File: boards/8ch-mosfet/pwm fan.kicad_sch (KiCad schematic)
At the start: 2 parts, among them M1 Fan_4pin

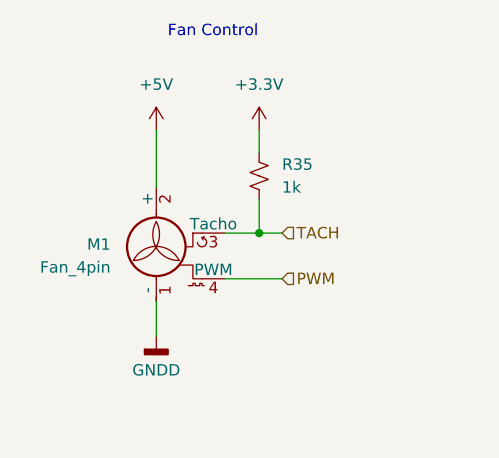
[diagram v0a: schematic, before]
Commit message: more or less placed all the stuff that needs to be placed
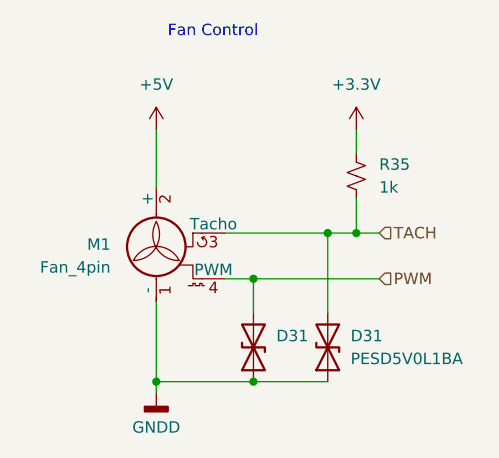
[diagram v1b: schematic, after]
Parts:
- added D31 (x2): PESD5V0L1BA, Diode_SMD:D_SOD-323_HandSoldering, symbol Device:D_TVS
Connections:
- net GNDD: now also D31.1 (A1), D31.1 (A1)
- net PWM: now also D31.2 (A2)
- net TACH: now also D31.2 (A2)
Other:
- moved on the sheet: R35
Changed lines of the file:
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@@
 (kicad_sch (version 20230121) (generator eeschema)
   (paper "A4")
-  (junction (at 144.78 85.09) (diameter 0) (color 0 0 0 0)
-  )
-  (wire (pts (xy 140.97 85.09) (xy 144.78 85.09))
-    (stroke (width 0) (type default))
-  )
-  (wire (pts (xy 144.78 85.09) (xy 147.32 85.09))
-    (stroke (width 0) (type default))
-  )
-  (wire (pts (xy 140.97 90.17) (xy 147.32 90.17))
-    (stroke (width 0) (type default))
-  )
-  (wire (pts (xy 144.78 81.28) (xy 144.78 85.09))
-    (stroke (width 0) (type default))
-  )
-  (wire (pts (xy 133.35 92.71) (xy 133.35 96.52))
-    (stroke (width 0) (type default))
-  )
-  (wire (pts (xy 144.78 76.2) (xy 144.78 73.66))
+  (junction (at 144.145 101.6) (diameter 0) (color 0 0 0 0)
+  )
+  (junction (at 152.4 85.09) (diameter 0) (color 0 0 0 0)
+  )
+  (junction (at 144.145 90.17) (diameter 0) (color 0 0 0 0)
+  )
+  (junction (at 155.575 85.09) (diameter 0) (color 0 0 0 0)
+  )
+  (junction (at 133.35 101.6) (diameter 0) (color 0 0 0 0)
+  )
+  (wire (pts (xy 152.4 85.09) (xy 155.575 85.09))
+    (stroke (width 0) (type default))
+  )
+  (wire (pts (xy 140.97 85.09) (xy 152.4 85.09))
+    (stroke (width 0) (type default))
+  )
+  (wire (pts (xy 155.575 85.09) (xy 158.115 85.09))
+    (stroke (width 0) (type default))
+  )
+  (wire (pts (xy 140.97 90.17) (xy 144.145 90.17))
+    (stroke (width 0) (type default))
+  )
+  (wire (pts (xy 155.575 81.28) (xy 155.575 85.09))
+    (stroke (width 0) (type default))
+  )
+  (wire (pts (xy 144.145 90.17) (xy 158.115 90.17))
+    (stroke (width 0) (type default))
+  )
+  (wire (pts (xy 144.145 101.6) (xy 152.4 101.6))
+    (stroke (width 0) (type default))
+  )
+  (wire (pts (xy 144.145 90.17) (xy 144.145 93.98))
+    (stroke (width 0) (type default))
+  )
+  (wire (pts (xy 133.35 92.71) (xy 133.35 101.6))
+    (stroke (width 0) (type default))
+  )
+  (wire (pts (xy 133.35 101.6) (xy 133.35 102.87))
+    (stroke (width 0) (type default))
+  )
+  (wire (pts (xy 155.575 76.2) (xy 155.575 73.66))
+    (stroke (width 0) (type default))
+  )
+  (wire (pts (xy 133.35 101.6) (xy 144.145 101.6))
     (stroke (width 0) (type default))
   )
   (wire (pts (xy 133.35 73.66) (xy 133.35 80.01))
+    (stroke (width 0) (type default))
+  )
+  (wire (pts (xy 152.4 85.09) (xy 152.4 93.98))
     (stroke (width 0) (type default))
   )
@@
     (effects (font (size 1.27 1.27)) (justify left bottom))
   )
-  (hierarchical_label "TACH" (shape input) (at 147.32 85.09 0) (fields_autoplaced)
+  (hierarchical_label "TACH" (shape input) (at 158.115 85.09 0) (fields_autoplaced)
     (effects (font (size 1.27 1.27)) (justify left))
   )
-  (hierarchical_label "PWM" (shape input) (at 147.32 90.17 0) (fields_autoplaced)
+  (hierarchical_label "PWM" (shape input) (at 158.115 90.17 0) (fields_autoplaced)
     (effects (font (size 1.27 1.27)) (justify left))
   )
-  (symbol (lib_id "Device:R_Small_US") (at 144.78 78.74 180) (unit 1)
+  (symbol (lib_id "Device:R_Small_US") (at 155.575 78.74 180) (unit 1)
     (in_bom yes) (on_board yes) (dnp no) (fields_autoplaced)
-    (property "Reference" "R35" (at 147.32 77.47 0)
-      (effects (font (size 1.27 1.27)) (justify right))
-    )
-    (property "Value" "1k" (at 147.32 80.01 0)
-      (effects (font (size 1.27 1.27)) (justify right))
-    )
-    (property "Footprint" "Resistor_SMD:R_0805_2012Metric_Pad1.20x1.40mm_HandSolder" (at 144.78 78.74 0)
-      (effects (font (size 1.27 1.27)) hide)
-    )
-    (property "Datasheet" "~" (at 144.78 78.74 0)
-      (effects (font (size 1.27 1.27)) hide)
-    )
-    (property "Vendor" "652-CR0805JW-103ELF" (at 144.78 78.74 0)
+    (property "Reference" "R35" (at 158.115 77.47 0)
+      (effects (font (size 1.27 1.27)) (justify right))
+    )
+    (property "Value" "1k" (at 158.115 80.01 0)
+      (effects (font (size 1.27 1.27)) (justify right))
+    )
+    (property "Footprint" "Resistor_SMD:R_0805_2012Metric_Pad1.20x1.40mm_HandSolder" (at 155.575 78.74 0)
+      (effects (font (size 1.27 1.27)) hide)
+    )
+    (property "Datasheet" "~" (at 155.575 78.74 0)
+      (effects (font (size 1.27 1.27)) hide)
+    )
+    (property "Vendor" "652-CR0805JW-103ELF" (at 155.575 78.74 0)
       (effects (font (size 1.27 1.27)) hide)
     )
@@
     )
   )
-  (symbol (lib_id "power:+3.3V") (at 144.78 73.66 0) (unit 1)
+  (symbol (lib_id "Device:D_TVS") (at 144.145 97.79 90) (unit 1)
+    (in_bom yes) (on_board yes) (dnp no)
+    (property "Reference" "D31" (at 146.685 96.52 90)
+      (effects (font (size 1.27 1.27)) (justify right))
+    )
+    (property "Value" "PESD5V0L1BA" (at 154.94 99.06 90)
+      (effects (font (size 1.27 1.27)) (justify right) hide)
+    )
+    (property "Footprint" "Diode_SMD:D_SOD-323_HandSoldering" (at 144.145 97.79 0)
+      (effects (font (size 1.27 1.27)) hide)
+    )
+    (property "Datasheet" "~" (at 144.145 97.79 0)
+      (effects (font (size 1.27 1.27)) hide)
+    )
+    (pin "1")
+    (pin "2")
+    (instances
+      (project "8ch-mosfet"
+        (path "/c83c6236-96e9-46ad-9d7a-9e2efa4a7966/0036d08f-39b5-4a29-8e4d-ea832b2cc879"
+          (reference "D31") (unit 1)
+        )
+        (path "/c83c6236-96e9-46ad-9d7a-9e2efa4a7966/e112a34f-fd2f-43cb-bf5d-a7f5e57b6bef"
+          (reference "D32") (unit 1)
+        )
+        (path "/c83c6236-96e9-46ad-9d7a-9e2efa4a7966/ad82ad0c-2ba8-4934-bb2a-ed6e11658eb2"
+          (reference "D34") (unit 1)
+        )
+        (path "/c83c6236-96e9-46ad-9d7a-9e2efa4a7966/02f6e629-b0e2-41e8-b2e4-f0e125a92a71"
+          (reference "D35") (unit 1)
+        )
+      )
+    )
+  )
+  (symbol (lib_id "power:+3.3V") (at 155.575 73.66 0) (unit 1)
     (in_bom yes) (on_board yes) (dnp no) (fields_autoplaced)
-    (property "Reference" "#PWR064" (at 144.78 77.47 0)
-      (effects (font (size 1.27 1.27)) hide)
-    )
-    (property "Value" "+3.3V" (at 144.78 68.58 0)
+    (property "Reference" "#PWR064" (at 155.575 77.47 0)
+      (effects (font (size 1.27 1.27)) hide)
+    )
+    (property "Value" "+3.3V" (at 155.575 68.58 0)
       (effects (font (size 1.27 1.27)))
     )
-    (property "Footprint" "" (at 144.78 73.66 0)
-      (effects (font (size 1.27 1.27)) hide)
-    )
-    (property "Datasheet" "" (at 144.78 73.66 0)
+    (property "Footprint" "" (at 155.575 73.66 0)
+      (effects (font (size 1.27 1.27)) hide)
+    )
+    (property "Datasheet" "" (at 155.575 73.66 0)
       (effects (font (size 1.27 1.27)) hide)
     )
@@
     )
   )
-  (symbol (lib_id "power:GNDD") (at 133.35 96.52 0) (unit 1)
+  (symbol (lib_id "power:GNDD") (at 133.35 102.87 0) (unit 1)
     (in_bom yes) (on_board yes) (dnp no) (fields_autoplaced)
-    (property "Reference" "#PWR08" (at 133.35 102.87 0)
-      (effects (font (size 1.27 1.27)) hide)
-    )
-    (property "Value" "GNDD" (at 133.35 100.33 0)
+    (property "Reference" "#PWR08" (at 133.35 109.22 0)
+      (effects (font (size 1.27 1.27)) hide)
+    )
+    (property "Value" "GNDD" (at 133.35 106.68 0)
       (effects (font (size 1.27 1.27)))
     )
-    (property "Footprint" "" (at 133.35 96.52 0)
-      (effects (font (size 1.27 1.27)) hide)
-    )
-    (property "Datasheet" "" (at 133.35 96.52 0)
+    (property "Footprint" "" (at 133.35 102.87 0)
+      (effects (font (size 1.27 1.27)) hide)
+    )
+    (property "Datasheet" "" (at 133.35 102.87 0)
       (effects (font (size 1.27 1.27)) hide)
     )
@@
         )
       )
+    )
+  )
+  (symbol (lib_id "Device:D_TVS") (at 152.4 97.79 90) (unit 1)
+    (in_bom yes) (on_board yes) (dnp no)
+    (property "Reference" "D31" (at 154.94 96.52 90)
+      (effects (font (size 1.27 1.27)) (justify right))
+    )
+    (property "Value" "PESD5V0L1BA" (at 154.94 99.06 90)
+      (effects (font (size 1.27 1.27)) (justify right))
+    )
+    (property "Footprint" "Diode_SMD:D_SOD-323_HandSoldering" (at 152.4 97.79 0)
+      (effects (font (size 1.27 1.27)) hide)
+    )
+    (property "Datasheet" "~" (at 152.4 97.79 0)
+      (effects (font (size 1.27 1.27)) hide)
+    )
+    (pin "1")
+    (pin "2")
+    (instances
+      (project "8ch-mosfet"
+        (path "/c83c6236-96e9-46ad-9d7a-9e2efa4a7966/0036d08f-39b5-4a29-8e4d-ea832b2cc879"
+          (reference "D31") (unit 1)
+        )
+        (path "/c83c6236-96e9-46ad-9d7a-9e2efa4a7966/e112a34f-fd2f-43cb-bf5d-a7f5e57b6bef"
+          (reference "D32") (unit 1)
+        )
+        (path "/c83c6236-96e9-46ad-9d7a-9e2efa4a7966/ad82ad0c-2ba8-4934-bb2a-ed6e11658eb2"
+          (reference "D36") (unit 1)
+        )
+        (path "/c83c6236-96e9-46ad-9d7a-9e2efa4a7966/02f6e629-b0e2-41e8-b2e4-f0e125a92a71"
+          (reference "D37") (unit 1)
+        )
+      )

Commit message: added in reverse polarity diode to power circuit
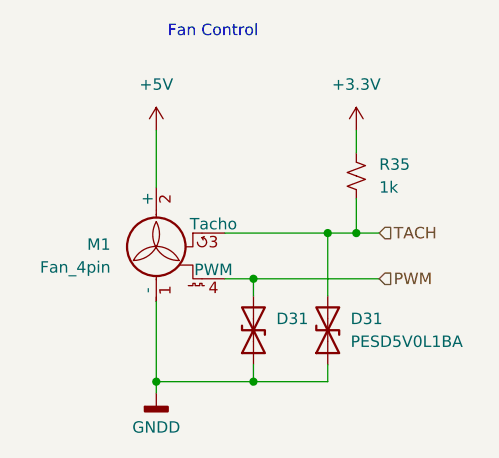
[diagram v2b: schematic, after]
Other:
- moved on the sheet: D31
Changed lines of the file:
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@@
+    (stroke (width 0) (type default))
+  )
+  (wire (pts (xy 152.4 101.6) (xy 152.4 99.695))
     (stroke (width 0) (type default))
   )
@@
     (stroke (width 0) (type default))
   )
+  (wire (pts (xy 144.145 99.695) (xy 144.145 101.6))
+    (stroke (width 0) (type default))
+  )
   (wire (pts (xy 144.145 101.6) (xy 152.4 101.6))
     (stroke (width 0) (type default))
   )
-  (wire (pts (xy 144.145 90.17) (xy 144.145 93.98))
+  (wire (pts (xy 144.145 90.17) (xy 144.145 92.075))
     (stroke (width 0) (type default))
   )
@@
     (stroke (width 0) (type default))
   )
-  (wire (pts (xy 152.4 85.09) (xy 152.4 93.98))
+  (wire (pts (xy 152.4 85.09) (xy 152.4 92.075))
     (stroke (width 0) (type default))
   )
@@
     )
   )
-  (symbol (lib_id "Device:D_TVS") (at 144.145 97.79 90) (unit 1)
+  (symbol (lib_id "Device:D_TVS") (at 144.145 95.885 90) (unit 1)
     (in_bom yes) (on_board yes) (dnp no)
-    (property "Reference" "D31" (at 146.685 96.52 90)
-      (effects (font (size 1.27 1.27)) (justify right))
-    )
-    (property "Value" "PESD5V0L1BA" (at 154.94 99.06 90)
+    (property "Reference" "D31" (at 146.685 94.615 90)
+      (effects (font (size 1.27 1.27)) (justify right))
+    )
+    (property "Value" "PESD5V0L1BA" (at 154.94 97.155 90)
       (effects (font (size 1.27 1.27)) (justify right) hide)
     )
-    (property "Footprint" "Diode_SMD:D_SOD-323_HandSoldering" (at 144.145 97.79 0)
-      (effects (font (size 1.27 1.27)) hide)
-    )
-    (property "Datasheet" "~" (at 144.145 97.79 0)
+    (property "Footprint" "Diode_SMD:D_SOD-323_HandSoldering" (at 144.145 95.885 0)
+      (effects (font (size 1.27 1.27)) hide)
+    )
+    (property "Datasheet" "~" (at 144.145 95.885 0)
       (effects (font (size 1.27 1.27)) hide)
     )
@@
     )
   )
-  (symbol (lib_id "Device:D_TVS") (at 152.4 97.79 90) (unit 1)
+  (symbol (lib_id "Device:D_TVS") (at 152.4 95.885 90) (unit 1)
     (in_bom yes) (on_board yes) (dnp no)
-    (property "Reference" "D31" (at 154.94 96.52 90)
-      (effects (font (size 1.27 1.27)) (justify right))
-    )
-    (property "Value" "PESD5V0L1BA" (at 154.94 99.06 90)
-      (effects (font (size 1.27 1.27)) (justify right))
-    )
-    (property "Footprint" "Diode_SMD:D_SOD-323_HandSoldering" (at 152.4 97.79 0)
-      (effects (font (size 1.27 1.27)) hide)
-    )
-    (property "Datasheet" "~" (at 152.4 97.79 0)
-      (effects (font (size 1.27 1.27)) hide)
-    )
+    (property "Reference" "D31" (at 154.94 94.615 90)
+      (effects (font (size 1.27 1.27)) (justify right))
+    )
+    (property "Value" "PESD5V0L1BA" (at 154.94 97.155 90)
+      (effects (font (size 1.27 1.27)) (justify right))
+    )
+    (property "Footprint" "Diode_SMD:D_SOD-323_HandSoldering" (at 152.4 95.885 0)
+      (effects (font (size 1.27 1.27)) hide)
+    )
+    (property "Datasheet" "~" (at 152.4 95.885 0)
+      (effects (font (size 1.27 1.27)) hide)
+    )

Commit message: tidied up the schematic
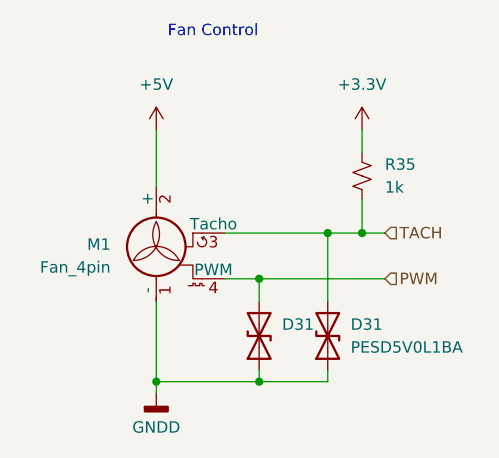
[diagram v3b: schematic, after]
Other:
- moved on the sheet: D31, R35
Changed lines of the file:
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@@
 (kicad_sch (version 20230121) (generator eeschema)
   (paper "A4")
-  (junction (at 144.145 101.6) (diameter 0) (color 0 0 0 0)
+  (junction (at 144.78 90.17) (diameter 0) (color 0 0 0 0)
+  )
+  (junction (at 144.78 101.6) (diameter 0) (color 0 0 0 0)
   )
   (junction (at 152.4 85.09) (diameter 0) (color 0 0 0 0)
   )
-  (junction (at 144.145 90.17) (diameter 0) (color 0 0 0 0)
-  )
-  (junction (at 155.575 85.09) (diameter 0) (color 0 0 0 0)
+  (junction (at 156.21 85.09) (diameter 0) (color 0 0 0 0)
   )
   (junction (at 133.35 101.6) (diameter 0) (color 0 0 0 0)
   )
-  (wire (pts (xy 152.4 85.09) (xy 155.575 85.09))
+  (wire (pts (xy 144.78 101.6) (xy 152.4 101.6))
+    (stroke (width 0) (type default))
+  )
+  (wire (pts (xy 152.4 85.09) (xy 156.21 85.09))
     (stroke (width 0) (type default))
   )
@@
     (stroke (width 0) (type default))
   )
-  (wire (pts (xy 152.4 101.6) (xy 152.4 99.695))
-    (stroke (width 0) (type default))
-  )
-  (wire (pts (xy 155.575 85.09) (xy 158.115 85.09))
-    (stroke (width 0) (type default))
-  )
-  (wire (pts (xy 140.97 90.17) (xy 144.145 90.17))
-    (stroke (width 0) (type default))
-  )
-  (wire (pts (xy 155.575 81.28) (xy 155.575 85.09))
-    (stroke (width 0) (type default))
-  )
-  (wire (pts (xy 144.145 90.17) (xy 158.115 90.17))
-    (stroke (width 0) (type default))
-  )
-  (wire (pts (xy 144.145 99.695) (xy 144.145 101.6))
-    (stroke (width 0) (type default))
-  )
-  (wire (pts (xy 144.145 101.6) (xy 152.4 101.6))
-    (stroke (width 0) (type default))
-  )
-  (wire (pts (xy 144.145 90.17) (xy 144.145 92.075))
+  (wire (pts (xy 152.4 101.6) (xy 152.4 100.33))
+    (stroke (width 0) (type default))
+  )
+  (wire (pts (xy 140.97 90.17) (xy 144.78 90.17))
+    (stroke (width 0) (type default))
+  )
+  (wire (pts (xy 156.21 81.28) (xy 156.21 85.09))
+    (stroke (width 0) (type default))
+  )
+  (wire (pts (xy 144.78 100.33) (xy 144.78 101.6))
+    (stroke (width 0) (type default))
+  )
+  (wire (pts (xy 156.21 85.09) (xy 158.75 85.09))
+    (stroke (width 0) (type default))
+  )
+  (wire (pts (xy 144.78 90.17) (xy 158.75 90.17))
+    (stroke (width 0) (type default))
+  )
+  (wire (pts (xy 144.78 90.17) (xy 144.78 92.71))
     (stroke (width 0) (type default))
   )
@@
     (stroke (width 0) (type default))
   )
-  (wire (pts (xy 155.575 76.2) (xy 155.575 73.66))
-    (stroke (width 0) (type default))
-  )
-  (wire (pts (xy 133.35 101.6) (xy 144.145 101.6))
+  (wire (pts (xy 156.21 73.66) (xy 156.21 76.2))
+    (stroke (width 0) (type default))
+  )
+  (wire (pts (xy 133.35 101.6) (xy 144.78 101.6))
     (stroke (width 0) (type default))
   )
@@
     (stroke (width 0) (type default))
   )
-  (wire (pts (xy 152.4 85.09) (xy 152.4 92.075))
+  (wire (pts (xy 152.4 85.09) (xy 152.4 92.71))
     (stroke (width 0) (type default))
   )
@@
     (effects (font (size 1.27 1.27)) (justify left bottom))
   )
-  (hierarchical_label "TACH" (shape input) (at 158.115 85.09 0) (fields_autoplaced)
+  (hierarchical_label "TACH" (shape input) (at 158.75 85.09 0) (fields_autoplaced)
     (effects (font (size 1.27 1.27)) (justify left))
   )
-  (hierarchical_label "PWM" (shape input) (at 158.115 90.17 0) (fields_autoplaced)
+  (hierarchical_label "PWM" (shape input) (at 158.75 90.17 0) (fields_autoplaced)
     (effects (font (size 1.27 1.27)) (justify left))
   )
-  (symbol (lib_id "Device:R_Small_US") (at 155.575 78.74 180) (unit 1)
-    (in_bom yes) (on_board yes) (dnp no) (fields_autoplaced)
-    (property "Reference" "R35" (at 158.115 77.47 0)
-      (effects (font (size 1.27 1.27)) (justify right))
-    )
-    (property "Value" "1k" (at 158.115 80.01 0)
-      (effects (font (size 1.27 1.27)) (justify right))
-    )
-    (property "Footprint" "Resistor_SMD:R_0805_2012Metric_Pad1.20x1.40mm_HandSolder" (at 155.575 78.74 0)
-      (effects (font (size 1.27 1.27)) hide)
-    )
-    (property "Datasheet" "~" (at 155.575 78.74 0)
-      (effects (font (size 1.27 1.27)) hide)
-    )
-    (property "Vendor" "652-CR0805JW-103ELF" (at 155.575 78.74 0)
+  (symbol (lib_id "Device:R_Small_US") (at 156.21 78.74 180) (unit 1)
+    (in_bom yes) (on_board yes) (dnp no) (fields_autoplaced)
+    (property "Reference" "R35" (at 158.75 77.47 0)
+      (effects (font (size 1.27 1.27)) (justify right))
+    )
+    (property "Value" "1k" (at 158.75 80.01 0)
+      (effects (font (size 1.27 1.27)) (justify right))
+    )
+    (property "Footprint" "Resistor_SMD:R_0805_2012Metric_Pad1.20x1.40mm_HandSolder" (at 156.21 78.74 0)
+      (effects (font (size 1.27 1.27)) hide)
+    )
+    (property "Datasheet" "~" (at 156.21 78.74 0)
+      (effects (font (size 1.27 1.27)) hide)
+    )
+    (property "Vendor" "652-CR0805JW-103ELF" (at 156.21 78.74 0)
       (effects (font (size 1.27 1.27)) hide)
     )
@@
     )
   )
-  (symbol (lib_id "Device:D_TVS") (at 144.145 95.885 90) (unit 1)
+  (symbol (lib_id "Device:D_TVS") (at 144.78 96.52 90) (unit 1)
     (in_bom yes) (on_board yes) (dnp no)
-    (property "Reference" "D31" (at 146.685 94.615 90)
-      (effects (font (size 1.27 1.27)) (justify right))
-    )
-    (property "Value" "PESD5V0L1BA" (at 154.94 97.155 90)
+    (property "Reference" "D31" (at 147.32 95.25 90)
+      (effects (font (size 1.27 1.27)) (justify right))
+    )
+    (property "Value" "PESD5V0L1BA" (at 155.575 97.79 90)
       (effects (font (size 1.27 1.27)) (justify right) hide)
     )
-    (property "Footprint" "Diode_SMD:D_SOD-323_HandSoldering" (at 144.145 95.885 0)
-      (effects (font (size 1.27 1.27)) hide)
-    )
-    (property "Datasheet" "~" (at 144.145 95.885 0)
+    (property "Footprint" "Diode_SMD:D_SOD-323_HandSoldering" (at 144.78 96.52 0)
+      (effects (font (size 1.27 1.27)) hide)
+    )
+    (property "Datasheet" "~" (at 144.78 96.52 0)
       (effects (font (size 1.27 1.27)) hide)
     )
@@
     )
   )
-  (symbol (lib_id "power:+3.3V") (at 155.575 73.66 0) (unit 1)
-    (in_bom yes) (on_board yes) (dnp no) (fields_autoplaced)
-    (property "Reference" "#PWR064" (at 155.575 77.47 0)
-      (effects (font (size 1.27 1.27)) hide)
-    )
-    (property "Value" "+3.3V" (at 155.575 68.58 0)
+  (symbol (lib_id "power:+3.3V") (at 156.21 73.66 0) (unit 1)
+    (in_bom yes) (on_board yes) (dnp no) (fields_autoplaced)
+    (property "Reference" "#PWR064" (at 156.21 77.47 0)
+      (effects (font (size 1.27 1.27)) hide)
+    )
+    (property "Value" "+3.3V" (at 156.21 68.58 0)
       (effects (font (size 1.27 1.27)))
     )
-    (property "Footprint" "" (at 155.575 73.66 0)
-      (effects (font (size 1.27 1.27)) hide)
-    )
-    (property "Datasheet" "" (at 155.575 73.66 0)
+    (property "Footprint" "" (at 156.21 73.66 0)
+      (effects (font (size 1.27 1.27)) hide)
+    )
+    (property "Datasheet" "" (at 156.21 73.66 0)
       (effects (font (size 1.27 1.27)) hide)
     )
@@
     )
   )
-  (symbol (lib_id "Device:D_TVS") (at 152.4 95.885 90) (unit 1)
+  (symbol (lib_id "Device:D_TVS") (at 152.4 96.52 90) (unit 1)
     (in_bom yes) (on_board yes) (dnp no)
-    (property "Reference" "D31" (at 154.94 94.615 90)
-      (effects (font (size 1.27 1.27)) (justify right))
-    )
-    (property "Value" "PESD5V0L1BA" (at 154.94 97.155 90)
-      (effects (font (size 1.27 1.27)) (justify right))
-    )
-    (property "Footprint" "Diode_SMD:D_SOD-323_HandSoldering" (at 152.4 95.885 0)
-      (effects (font (size 1.27 1.27)) hide)
-    )
-    (property "Datasheet" "~" (at 152.4 95.885 0)
-      (effects (font (size 1.27 1.27)) hide)
-    )
+    (property "Reference" "D31" (at 154.94 95.25 90)
+      (effects (font (size 1.27 1.27)) (justify right))
+    )
+    (property "Value" "PESD5V0L1BA" (at 154.94 97.79 90)
+      (effects (font (size 1.27 1.27)) (justify right))
+    )
+    (property "Footprint" "Diode_SMD:D_SOD-323_HandSoldering" (at 152.4 96.52 0)
+      (effects (font (size 1.27 1.27)) hide)
+    )
+    (property "Datasheet" "~" (at 152.4 96.52 0)
+      (effects (font (size 1.27 1.27)) hide)
+    )

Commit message: fixed a part number
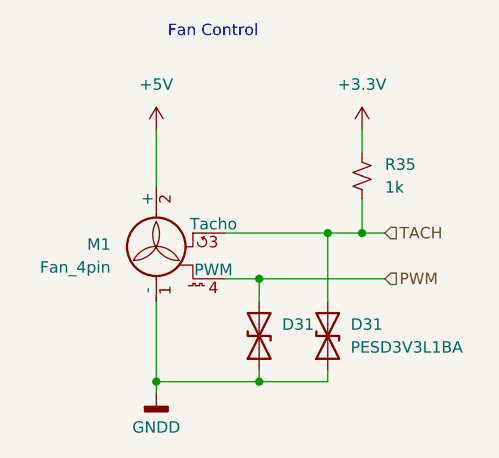
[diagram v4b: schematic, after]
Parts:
- D31: value PESD5V0L1BA -> PESD3V3L1BA
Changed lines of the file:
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@@
       (effects (font (size 1.27 1.27)) (justify right))
     )
-    (property "Value" "PESD5V0L1BA" (at 155.575 97.79 90)
+    (property "Value" "PESD3V3L1BA" (at 155.575 97.79 90)
       (effects (font (size 1.27 1.27)) (justify right) hide)
     )
@@
       (effects (font (size 1.27 1.27)) (justify right))
     )
-    (property "Value" "PESD5V0L1BA" (at 154.94 97.79 90)
+    (property "Value" "PESD3V3L1BA" (at 154.94 97.79 90)
       (effects (font (size 1.27 1.27)) (justify right))
     )
